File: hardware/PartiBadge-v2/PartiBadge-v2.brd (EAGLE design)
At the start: 119.8 x 118.6 mm, 32 parts, among them J1 I2C, J2 Supply

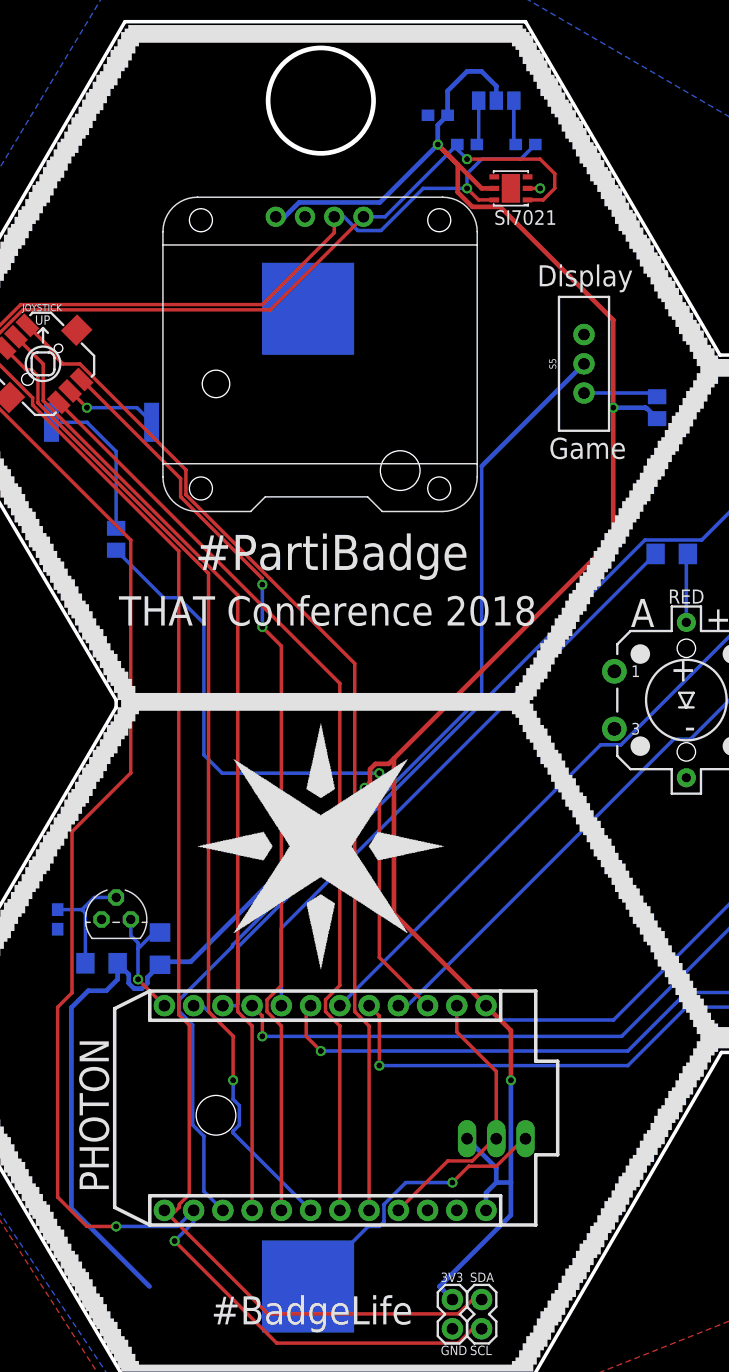
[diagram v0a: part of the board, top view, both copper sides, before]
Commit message: fixed power routing and made 3V3 traces wider
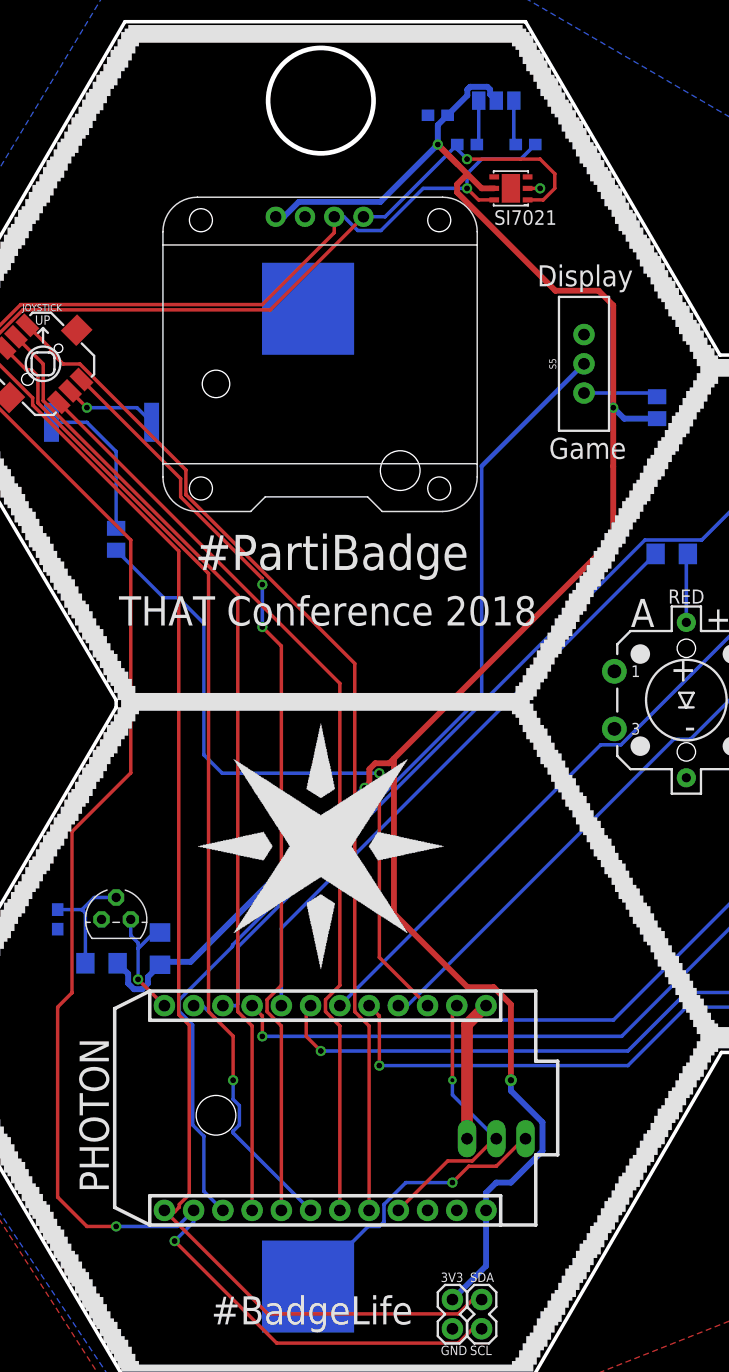
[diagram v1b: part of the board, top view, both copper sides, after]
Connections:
- new net 5V: IC1.OUT, PHOTON.1
- net +3V3: no longer IC1.OUT, PHOTON.1
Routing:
- net +3V3: track 239.3 -> 198.3 mm
- net 5V: track 0.00 -> 12.2 mm
- net GND: track 33.4 -> 33.7 mm, vias 2 -> 3

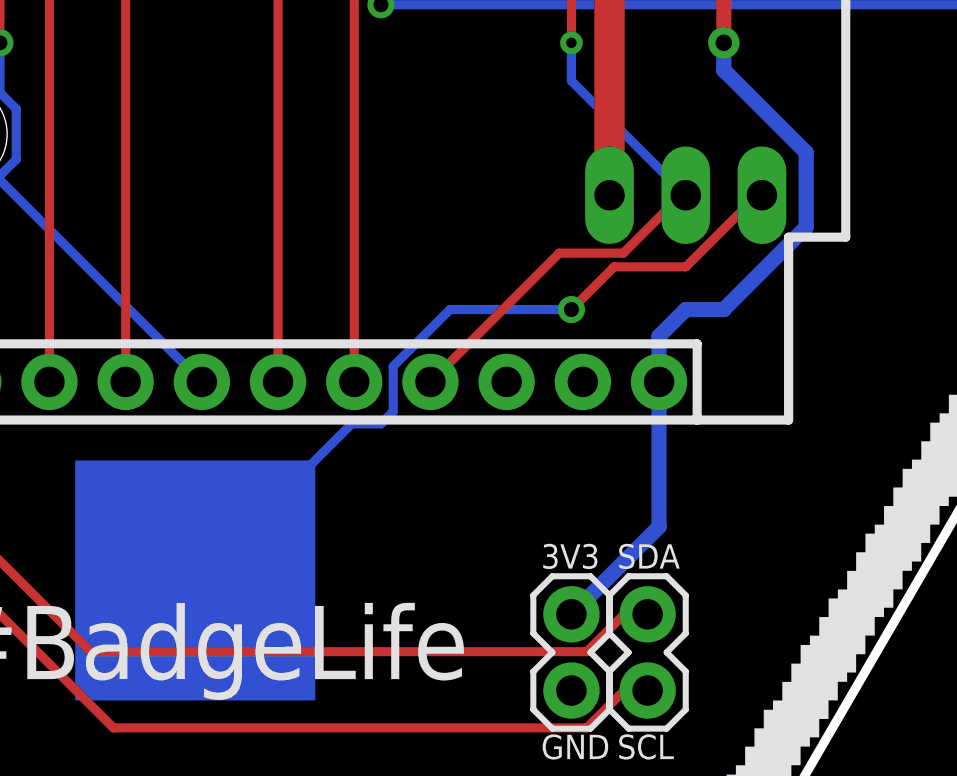
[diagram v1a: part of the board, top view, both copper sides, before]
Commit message: widened traces from batt to converter
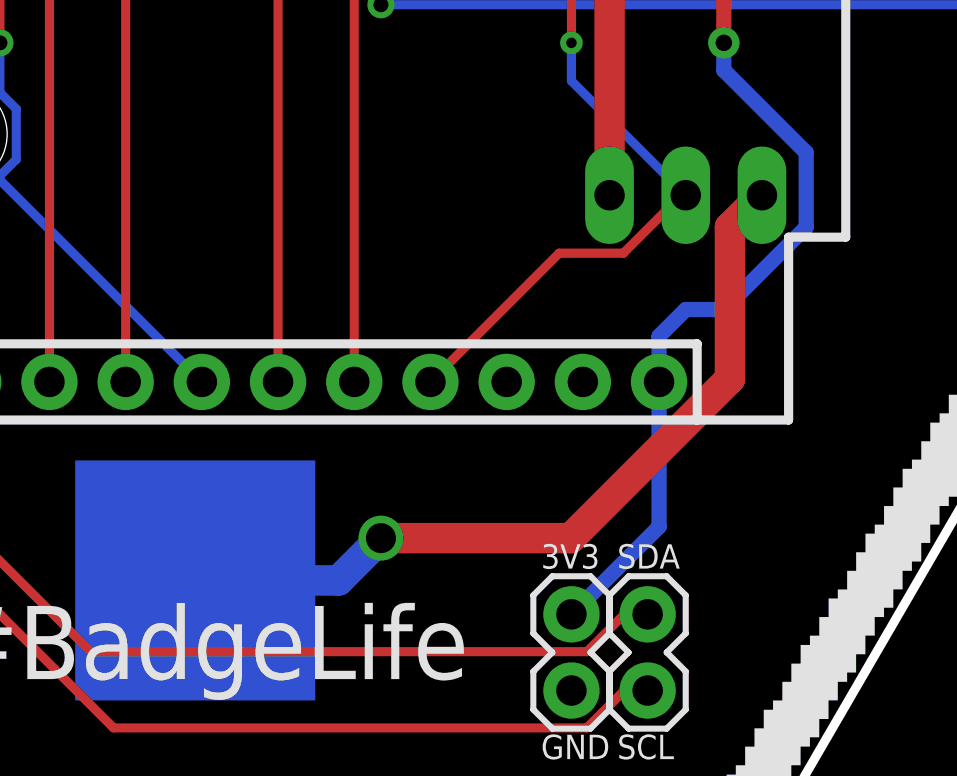
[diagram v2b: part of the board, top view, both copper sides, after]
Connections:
- net N$5 renamed VIN
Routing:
- net VIN: track 25.1 -> 27.3 mm
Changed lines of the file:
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@@
 <wire x1="66.99" y1="88.9" x2="67.31" y2="88.58" width="0.3048" layer="16"/>
-</signal>
-<signal name="N$5">
-<contactref element="U$2" pad="BATTERY_POSITIVE"/>
-<contactref element="IC1" pad="IN"/>
-<wire x1="36.99" y1="11.29" x2="42.21" y2="16.51" width="0.3048" layer="16"/>
-<wire x1="42.21" y1="16.51" x2="43.18" y2="16.51" width="0.3048" layer="16"/>
-<wire x1="43.18" y1="16.51" x2="43.5864" y2="16.9164" width="0.3048" layer="16"/>
-<wire x1="43.5864" y1="16.9164" x2="43.5864" y2="18.42253125" width="0.3048" layer="16"/>
-<wire x1="43.5864" y1="18.42253125" x2="45.48386875" y2="20.32" width="0.3048" layer="16"/>
-<wire x1="45.48386875" y1="20.32" x2="49.53" y2="20.32" width="0.3048" layer="16"/>
-<via x="49.53" y="20.32" extent="1-16" drill="0.5"/>
-<wire x1="49.53" y1="20.32" x2="50.9524" y2="21.7424" width="0.3048" layer="1"/>
-<wire x1="55.73333125" y1="24.13" x2="55.88" y2="24.13" width="0.3048" layer="1"/>
-<wire x1="50.9524" y1="21.7424" x2="53.34573125" y2="21.7424" width="0.3048" layer="1"/>
-<wire x1="53.34573125" y1="21.7424" x2="55.73333125" y2="24.13" width="0.3048" layer="1"/>
 </signal>
 <signal name="5V">
@@
 <wire x1="50.8" y1="34.036" x2="50.8" y2="24.13" width="1.016" layer="1"/>
 </signal>
+<signal name="VIN">
+<contactref element="U$2" pad="BATTERY_POSITIVE"/>
+<contactref element="IC1" pad="IN"/>
+<wire x1="55.73333125" y1="24.13" x2="55.88" y2="24.13" width="0.3048" layer="1"/>
+<wire x1="55.88" y1="24.13" x2="54.8132" y2="23.0632" width="1.016" layer="1"/>
+<wire x1="54.8132" y1="23.0632" x2="54.8132" y2="18.006175" width="1.016" layer="1"/>
+<wire x1="54.8132" y1="18.006175" x2="49.507025" y2="12.7" width="1.016" layer="1"/>
+<wire x1="49.507025" y1="12.7" x2="43.18" y2="12.7" width="1.016" layer="1"/>
+<via x="43.18" y="12.7" extent="1-16" drill="1"/>
+<wire x1="36.99" y1="11.29" x2="41.77" y2="11.29" width="1.016" layer="16"/>
+<wire x1="41.77" y1="11.29" x2="43.18" y2="12.7" width="1.016" layer="16"/>
+</signal>
 </signals>

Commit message: fix v2 board issues
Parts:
- removed TSMP58000: IR Sensor, transistor-npn:TO92
- removed U$2: SMT18650, SMT18650:18650SMT
- added IC2: TSMP58000, TSMP58000:TSMP58000
- added U1: 1042, 1042:KEYSTONE-1042
- moved J1 92.5 mm to (104.8, 86.2)
- moved J2 92.5 mm to (102.2, 83.7)
- flipped PARTIFRAME to the bottom
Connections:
- removed net VIN: IC1.IN, U$2.BATTERY_POSITIVE
- new net BATT: IC1.IN, U1.2
- net BUTTON_B: now also PHOTON.7; no longer PHOTON.6
- net BUTTON_G: now also PHOTON.6; no longer PHOTON.5
- net BUTTON_R: now also PHOTON.5; no longer PHOTON.4
- net BUTTON_Y: now also PHOTON.8; no longer PHOTON.7
- net GND: now also IC2.2, U1.1; no longer TSMP58000.3, U$2.BATTERY_NEGATIVE
- net IR_RECEIVER: now also IC2.1, PHOTON.4; no longer PHOTON.12, TSMP58000.1
- net LED_B: now also PHOTON.11; no longer PHOTON.10
- net LED_G: now also PHOTON.10; no longer PHOTON.9
- net LED_R: now also PHOTON.9; no longer PHOTON.8
- net LED_Y: now also PHOTON.12; no longer PHOTON.11
- net N$9: now also IC2.3; no longer TSMP58000.2
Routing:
- net IR_RECEIVER: track 11.2 -> 183.7 mm, vias 1 -> 2
- net BATT: track 0.00 -> 31.4 mm, vias 0 -> 1
- net +3V3: track 198.3 -> 228.9 mm
- net SCL: track 190.7 -> 219.4 mm, vias 3 -> 2
- net VIN: track 27.3 -> 0.00 mm, vias 1 -> 0
- net SDA: track 177.5 -> 202.2 mm
- net LED_Y: track 69.1 -> 80.3 mm, vias 0 -> 2
- net N$9: track 10.3 -> 19.8 mm
- net BUTTON_R: track 43.3 -> 45.8 mm
- net BUTTON_B: track 76.4 -> 79.0 mm
- net BUTTON_G: track 91.8 -> 94.2 mm
- net LED_G: track 94.4 -> 96.6 mm
- net LED_R: track 52.7 -> 53.8 mm
- net BUTTON_Y: track 69.9 -> 70.6 mm
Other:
- board size 119.8 x 118.6 mm -> 118.9 x 117.7 mm

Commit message: mode switch to power and other cosmetic changes
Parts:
- removed R8: 100, rcl:M0805
- moved S5 46.2 mm to (54.6, 45.7), turned to 90 degrees
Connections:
- removed net N$2: PHOTON.15, S5.2
- removed net N$3: R8.1, S5.3
- new net NC: S5.3
- new net ON: IC1.IN, S5.1
- net +3V3: no longer R8.2
- net BATT: now also S5.2; no longer IC1.IN
- net CENT: now also PHOTON.15; no longer PHOTON.16
- net DOWN: now also PHOTON.18; no longer PHOTON.19
- net GND: no longer S5.1
- net LEFT: now also PHOTON.17; no longer PHOTON.18
- net RIGHT: now also PHOTON.16; no longer PHOTON.17
- net UP: now also PHOTON.19; no longer PHOTON.20
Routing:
- net IR_RECEIVER: track 183.7 -> 57.9 mm
- net N$2: track 89.7 -> 0.00 mm
- net BATT: track 31.4 -> 56.5 mm
- net ON: track 0.00 -> 23.2 mm
- net N$3: track 6.48 -> 0.00 mm
- net BUTTON_R: track 45.8 -> 48.6 mm
- net +3V3: track 228.9 -> 231.5 mm
- net LEFT: track 86.3 -> 85.1 mm
- net DOWN: track 81.3 -> 82.4 mm
- net UP: track 90.0 -> 91.1 mm
- net RIGHT: track 80.4 -> 81.4 mm
- net CENT: track 84.4 -> 85.4 mm
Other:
- board text added: "Off"
- board text added: "On"
- board text removed: "Display"
- board text removed: "Game"
